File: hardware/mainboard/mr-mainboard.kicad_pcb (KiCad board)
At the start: 6 copper layers, 70 x 90 mm, 177 parts, among them J1 Conn_01x40_Shielded, J2 Conn_01x40_Shielded, J3 EAR, J4 Conn_02x06_Top_Bottom, P1 M2_SOCKET_E, Q1 2N7002, SW1 SW_Push, SW2 SW_Push, U1 LIFCL_40_CABGA400, U10 Si52112-B, U11 EM6GA16LBXA-12H, U2 TPS65632R, U3 TLV71330PDBV, U4 TPS62822, U5 TPS62822, U6 TPS62822, U7 W25Q128JVS, U8 ICM-20948, U9 74AHC1G126, X1 XO32, Y1 25MHz

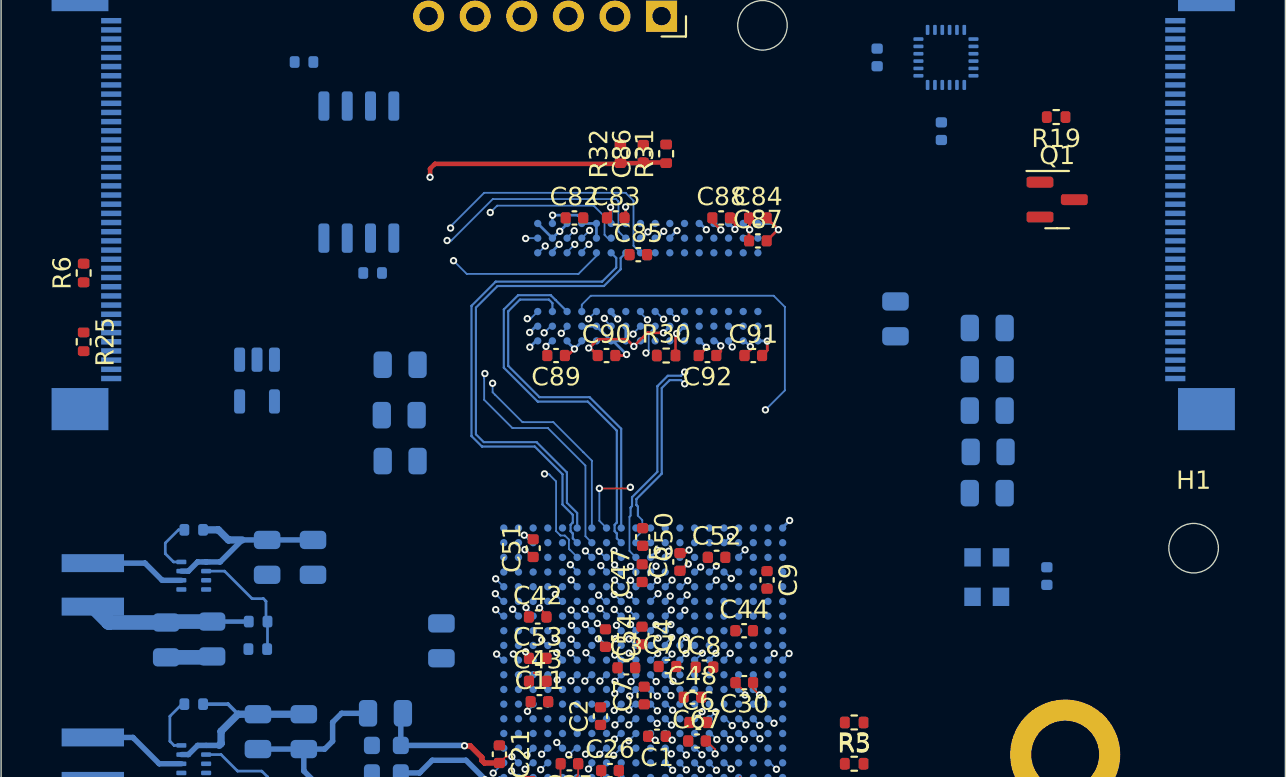
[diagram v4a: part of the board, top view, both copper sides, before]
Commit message: Interboard pair routing
Signed-off-by: David Shah <dave@ds0.me>
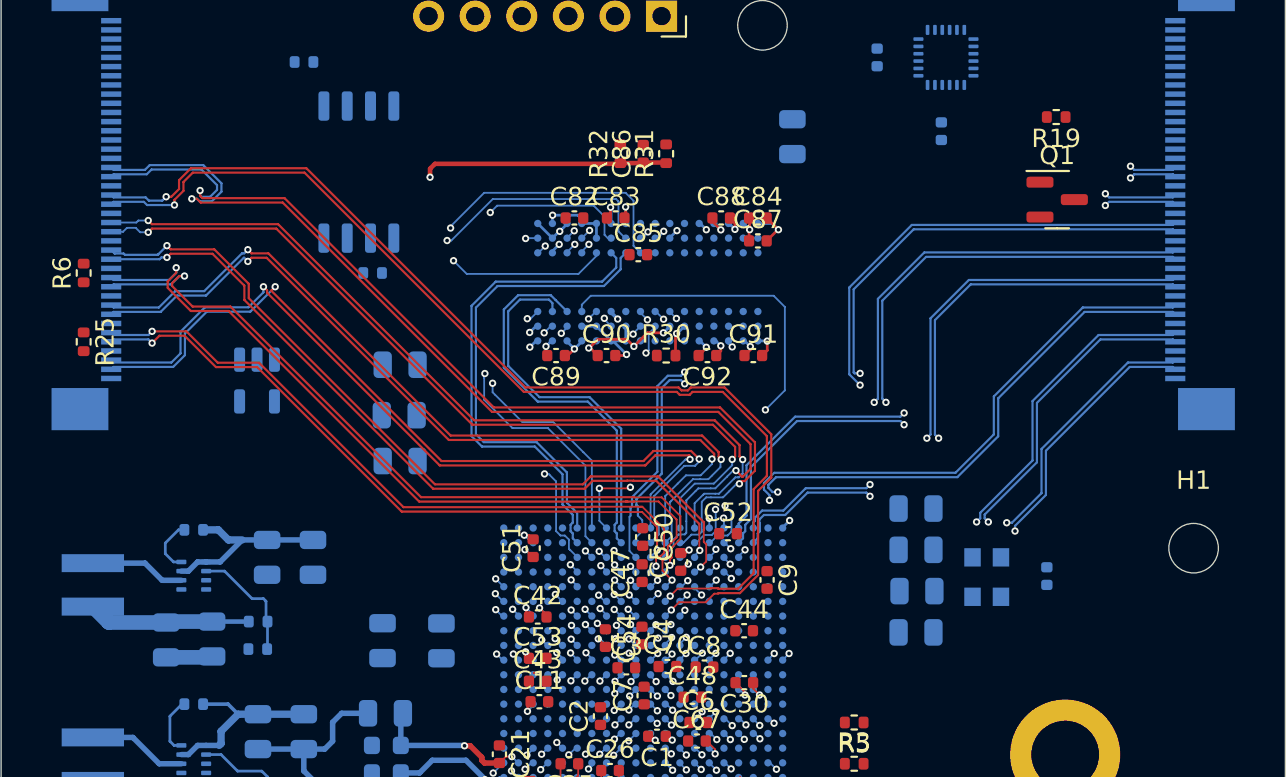
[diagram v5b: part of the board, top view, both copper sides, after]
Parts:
- moved C10 37.1 mm to (80.8, 147.0), turned to -90 degrees
- moved C39 11.4 mm to (103.1, 119.6)
- moved C12 8.52 mm to (109.9, 139.8)
- moved C13 8.52 mm to (109.9, 146.6)
- moved C46 8.52 mm to (109.9, 144.3)
- moved C49 8.52 mm to (109.9, 142.1)
- moved C52 1.43 mm to (99.6, 141.2)
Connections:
- J2 pad 27: B2BR_CLKI+ -> B2BR_DO2+
- U1 pad P12: B2BL_DO0- -> B2BL_DO1-
- U1 pad R12: B2BL_DO0+ -> B2BL_DO1+
- U1 pad T12: B2BL_DI2- -> B2BL_DI1-
- U1 pad U12: B2BL_DI1- -> B2BL_DI1+
- U1 pad U14: B2BL_DO2- -> B2BL_DI2-
- U1 pad U15: B2BR_DI1- -> B2BR_CLKO+
- U1 pad V12: B2BL_DI2+ -> B2BL_DO2-
- U1 pad V14: B2BL_DO2+ -> B2BL_DI2+
- U1 pad W13: B2BL_DI1+ -> B2BL_DO2+
- U1 pad Y13: B2BL_DO1+ -> B2BL_DO0+
- U1 pad Y14: B2BL_DO1- -> B2BL_DO0-
- U1 pad Y16: B2BR_CLKO+ -> B2BR_DI1-
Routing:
- net B2BR_DI0+: track 0.56 -> 61.7 mm, vias 1 -> 2
- net B2BR_DI0-: track 0.00 -> 60.2 mm, vias 0 -> 2
- net B2BL_DO1-: track 0.00 -> 57.2 mm, vias 0 -> 2
- net B2BL_DO1+: track 0.00 -> 56.4 mm, vias 0 -> 2
- net B2BL_DO2-: track 0.44 -> 54.5 mm, vias 1 -> 2
- net B2BR_DI2-: track 0.53 -> 53.8 mm, vias 1 -> 2
- net B2BL_DO2+: track 0.00 -> 52.3 mm, vias 0 -> 2
- net B2BR_DI2+: track 0.43 -> 51.1 mm, vias 1 -> 2
- net B2BL_CLKO-: track 0.00 -> 46.0 mm, vias 0 -> 2
- net B2BL_CLKI+: track 0.00 -> 45.6 mm, vias 0 -> 2
- net B2BL_DO0-: track 0.47 -> 45.8 mm, vias 1 -> 2
- net B2BL_DO0+: track 0.40 -> 45.5 mm, vias 1 -> 2
- net B2BL_CLKO+: track 0.00 -> 44.4 mm, vias 0 -> 2
- net B2BL_CLKI-: track 0.00 -> 43.5 mm, vias 0 -> 2
- net B2BL_DI1-: track 0.00 -> 42.8 mm, vias 0 -> 2
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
